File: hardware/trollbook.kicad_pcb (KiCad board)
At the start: 2 copper layers, 100 x 100 mm, 30 parts, among them U1 XC95288-208, U2 MC68030, U3 MC68882, U4 IDT71V416, U7 39F040, U8 MCP660

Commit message: dram
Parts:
- removed DB9FC: VAL**, DB9FC
- removed R10, R11, R12, R13, R14, R15, R16, R4, R5, R6, R7, R8, R9: R, SM0805
- added J2: VGAF, SUPER_CAP, F.Cu at (45.4, 237.8)
- added RP5: 10k, RPACK8_SMD, F.Cu at (73.5, 261.2)
- added RP6: 10k, RPACK8_SMD, F.Cu at (62.0, 246.7)
- added RP7: 10k, RPACK8_SMD, F.Cu at (72.6, 214.3)
- added RP8: 10k, RPACK8_SMD, F.Cu at (26.8, 232.6)
- added U10: 74LS574, SO20L, F.Cu at (80.4, 183.8)
- added U11: 74LS574, SO20L, B.Cu at (109.7, 169.3)
- added U12: HY57V561620, TSOP54, F.Cu at (178.1, 198.0)
- added U13: HY57V561620, TSOP54, F.Cu at (178.2, 182.5)
- added U6: 74LS574, SO20L, F.Cu at (98.1, 151.1)
- added U9: 74LS574, SO20L, B.Cu at (103.8, 195.5)
- R1, R2, R3: value R -> 10k
- RP1, RP2, RP3, RP4: value R_PACK4 -> 20k
- moved R19 153.4 mm to (16.1, 220.4)
- moved R17 153.4 mm to (41.3, 216.8)
- moved R18 153.4 mm to (34.4, 217.5)
- moved R2 153.4 mm to (16.0, 224.9)
- moved R3 153.4 mm to (27.5, 218.4)
- moved U8 153.4 mm to (37.1, 224.8)
- moved R1 153.4 mm to (16.3, 222.6)
- moved RP2 142.8 mm to (61.8, 252.3)
- moved RP4 140.0 mm to (61.0, 237.5)
- moved RP1 130.5 mm to (73.5, 264.8)
- moved RP3 126.7 mm to (72.5, 218.2)
- moved U4 1.95 mm to (106.9, 181.9)
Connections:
- R1 pad 1: N-0000013 -> N-00000162
- R1 pad 2: N-0000035 -> GND
- R2 pad 1: N-0000035 -> N-00000161
- R2 pad 2: N-0000090 -> GND
- R3 pad 1: N-0000090 -> N-00000160
- R3 pad 2: N-0000039 -> GND
- RP1 pad 1: (no net) -> N-000001
- RP1 pad 2: (no net) -> N-00000168
- RP1 pad 3: (no net) -> N-000005
- RP1 pad 4: (no net) -> N-00000167
- RP1 pad 5: N-0000039 -> /VGAB1
- RP1 pad 6: N-0000090 -> /VGAB2
- RP1 pad 7: N-0000035 -> /VGAB3
- RP1 pad 8: N-0000013 -> /VGAB4
- RP2 pad 1: (no net) -> N-00000166
- RP2 pad 2: (no net) -> N-000004
- RP2 pad 3: (no net) -> N-00000165
- RP2 pad 4: (no net) -> N-00000164
- RP2 pad 5: N-0000018 -> /VGAG3
- RP2 pad 6: N-000007 (its old number) -> /VGAG4
- RP2 pad 7: N-0000016 -> /VGAG5
- RP2 pad 8: N-0000017 -> /VGAB0
- RP3 pad 1: (no net) -> N-000002
- RP3 pad 2: (no net) -> N-00000163
- RP3 pad 3: (no net) -> N-00000159
- RP3 pad 4: (no net) -> N-000009
- RP3 pad 5: N-0000015 -> /VGAR4
- RP3 pad 6: N-0000010 (its old number) -> /VGAG0
- RP3 pad 7: N-000009 -> /VGAG1
- RP3 pad 8: N-000008 (its old number) -> /VGAG2
- RP4 pad 1: (no net) -> N-00000158
- RP4 pad 2: (no net) -> N-00000157
- RP4 pad 3: (no net) -> N-000003
- RP4 pad 4: (no net) -> N-00000169
- RP4 pad 5: N-0000012 (its old number) -> /VGAR0
- RP4 pad 6: N-0000091 -> /VGAR1
- RP4 pad 7: N-0000092 -> /VGAR2
- RP4 pad 8: N-0000011 (its old number) -> /VGAR3
- U1 pad 100: (no net) -> /FC1
- U1 pad 101: (no net) -> /FC2
- U1 pad 128: (no net) -> /DSACK0
- U1 pad 131: (no net) -> /DSACK1
- U1 pad 138: (no net) -> /CBACK
- U1 pad 139: (no net) -> /CBREQ
- U1 pad 140: (no net) -> /AS
- U1 pad 142: (no net) -> /DS
- U1 pad 164: (no net) -> /RW
- U1 pad 165: (no net) -> /SIZ1
- U1 pad 166: (no net) -> /SIZ0
- U1 pad 167: (no net) -> /DBEN
- U1 pad 99: (no net) -> /FC0
- U2 pad 10: (no net) -> /FC1
- U2 pad 117: (no net) -> /RW
- U2 pad 119: (no net) -> /SIZ1
- U2 pad 12: (no net) -> /FC0
- U2 pad 120: (no net) -> /SIZ0
- U2 pad 121: (no net) -> /DBEN
- U2 pad 124: (no net) -> /DS
- U2 pad 125: (no net) -> /AS
- U2 pad 126: (no net) -> /CBREQ
- U2 pad 127: (no net) -> /CBACK
- U2 pad 129: (no net) -> +5V
- U2 pad 132: (no net) -> /DSACK1
- U2 pad 17: (no net) -> +5V
- U2 pad 3: (no net) -> /DSACK0
- U2 pad 9: (no net) -> /FC2
- U3 pad 18: (no net) -> +5V
- U3 pad 20: (no net) -> /DS
- U3 pad 21: (no net) -> /AS
- U3 pad 26: /A0 -> +5V
- U3 pad 28: (no net) -> /RW
- U3 pad 31: (no net) -> /DSACK1
- U3 pad 32: (no net) -> /DSACK0
- U7 pad 31: (no net) -> /RW
- U8 pad 10: N-0000016 -> N-000004
- U8 pad 12: N-0000015 -> N-000009
- U8 pad 5: N-0000013 -> N-000001
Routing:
- net /RAMA11: track 0.00 -> 15.8 mm
- net /RAMA7: track 0.00 -> 15.8 mm
- net /RAMA2: track 0.00 -> 15.8 mm
- net /RAMD12: track 0.00 -> 15.8 mm
- net /RAMD11: track 0.00 -> 15.8 mm
- net /RAMB0: track 0.00 -> 15.8 mm
- net /RAMWE: track 0.00 -> 15.8 mm
- net /RAMLDQM: track 0.00 -> 15.8 mm
- net /RAMUDQM: track 0.00 -> 15.8 mm
- net /RAMD6: track 0.00 -> 15.8 mm
- net /RAMCKE: track 0.00 -> 15.8 mm
- net /RAMA12: track 0.00 -> 15.8 mm
- net /RAMD3: track 0.00 -> 15.8 mm
- net /RAMA8: track 0.00 -> 15.8 mm
- net /RAMD2: track 0.00 -> 15.8 mm
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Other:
- net class ninja added: clearance 0.1524, trace_width 0.1524, via_dia 0.7, via_drill 0.3
- rule trace_min: 0.2032 -> 0.1524

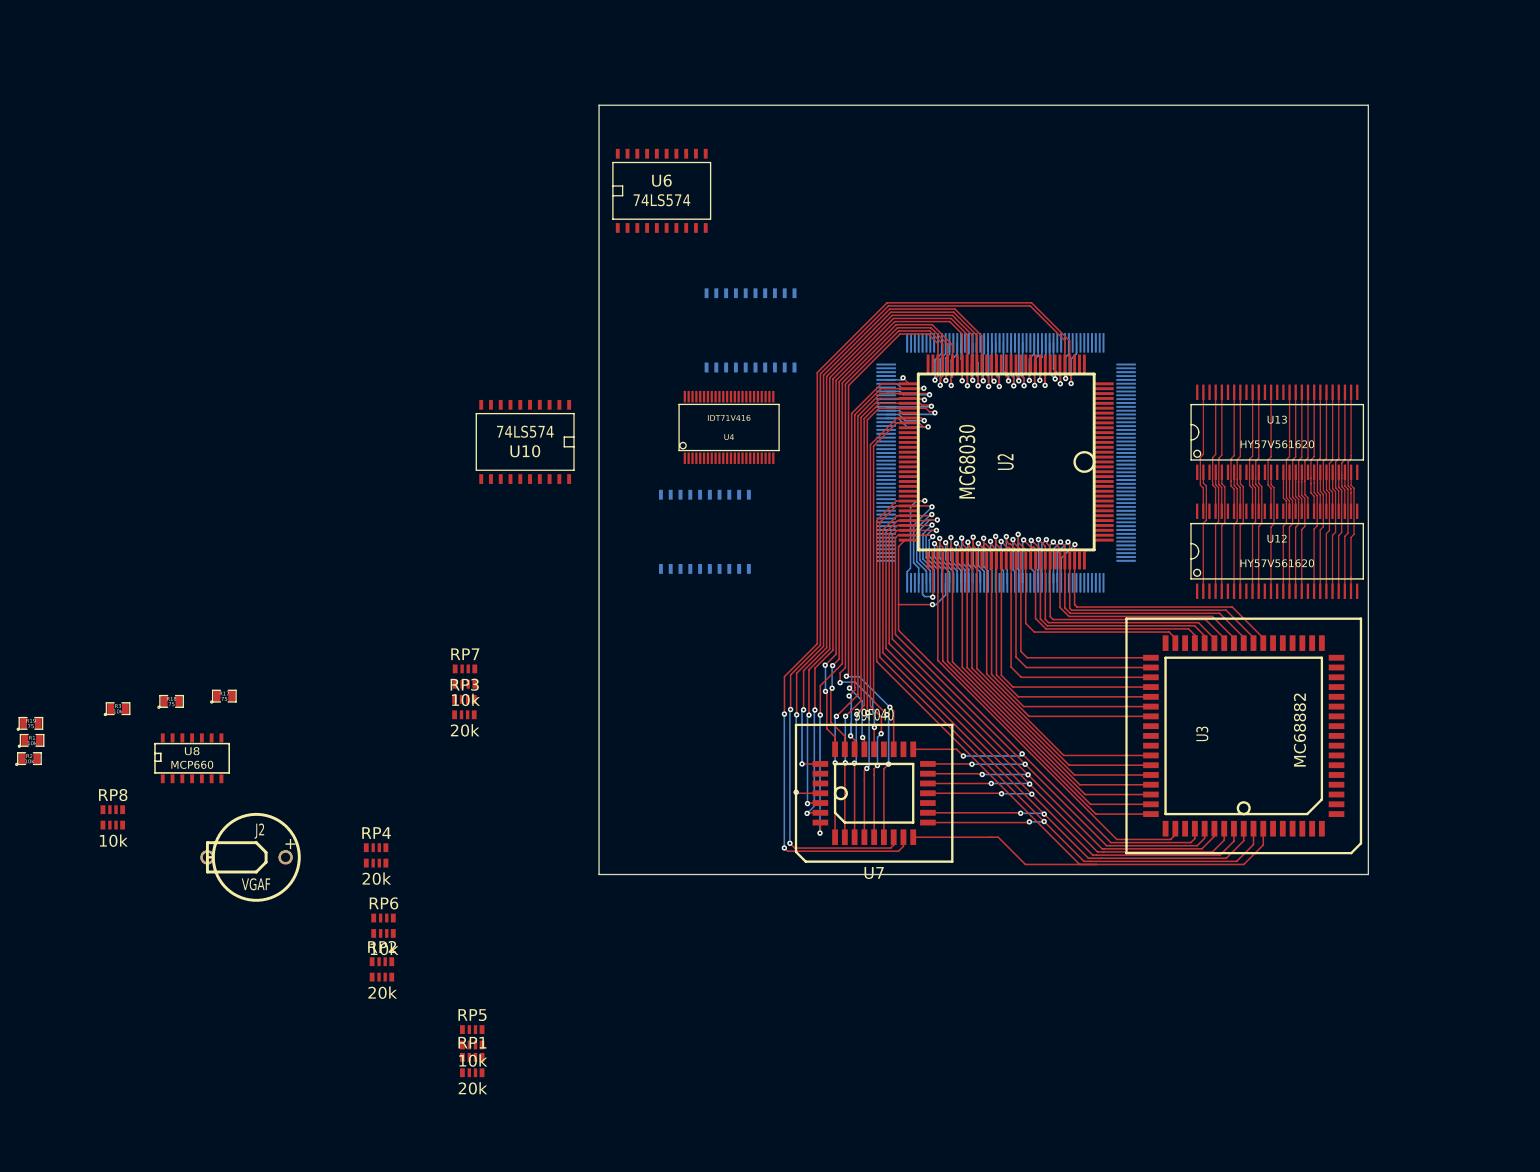
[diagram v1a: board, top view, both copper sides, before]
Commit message: routed sram, dram
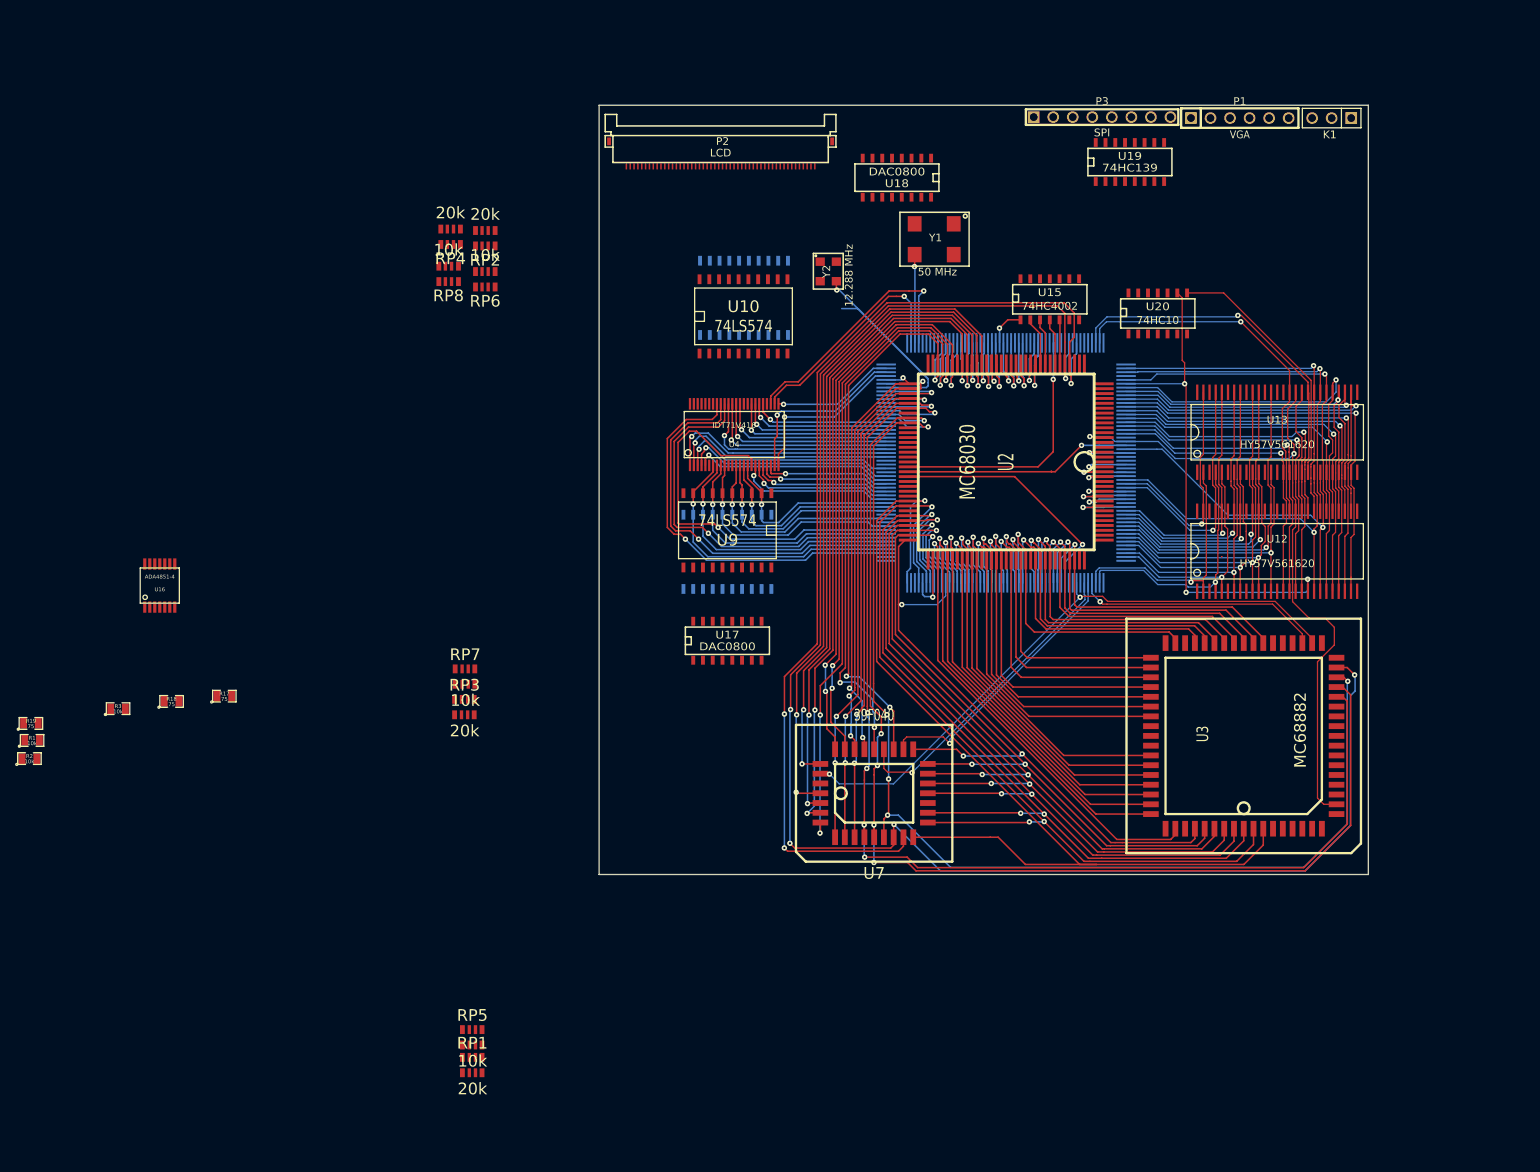
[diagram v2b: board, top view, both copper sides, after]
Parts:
- removed J2: VGAF, SUPER_CAP
- removed U8: MCP660, SO14E
- added K1: CONN_3, PIN_ARRAY_3X1, F.Cu at (185.2, 141.7)
- added P1: VGA, PIN_ARRAY-6X1, F.Cu at (173.3, 141.7)
- added P2: LCD, FH12-50S-0.5SH, F.Cu at (118.0, 147.4)
- added P3: SPI, pin_array_8x1, F.Cu at (155.4, 140.3)
- added U15: 74HC4002, SO14E, F.Cu at (148.6, 165.1)
- added U16: ADA4851-4, tssop-14, F.Cu at (32.9, 202.4)
- added U17: DAC0800, SO16E, F.Cu at (106.7, 209.6)
- added U18: DAC0800, SO16E, F.Cu at (128.7, 149.4)
- added U19: 74HC139, SO16E, F.Cu at (159.0, 147.4)
- added U20: 74HC10, SO14E, F.Cu at (162.6, 166.9)
- added Y1: 50 MHz, OSC-VCC1-B3B, F.Cu at (133.6, 157.4)
- added Y2: 12.288 MHz, OSC-ASFLMB, F.Cu at (119.8, 161.6)
- U6: moved to B.Cu
- U9: moved to F.Cu
- moved RP2 96.0 mm to (75.2, 157.3), turned to 180 degrees
- moved RP6 85.1 mm to (75.2, 162.6), turned to 180 degrees
- moved RP8 83.0 mm to (70.4, 161.9), turned to 180 degrees
- moved RP4 81.0 mm to (70.7, 157.1), turned to 180 degrees
- moved U6 47.7 mm to (106.7, 198.1)
- moved U10 32.7 mm to (108.8, 167.4), turned to 0 degrees
- moved U11 4.31 mm to (108.8, 165.0)
- moved U9 2.93 mm to (106.7, 195.3), turned to 180 degrees
- moved U4 1.15 mm to (107.6, 182.8)
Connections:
- U1 pad 100: /FC1 -> /SSBIN1
- U1 pad 101: /FC2 -> /CPUMODE
- U1 pad 102: (no net) -> /RAMA12
- U1 pad 103: (no net) -> /RAMUDQM
- U1 pad 106: (no net) -> /RAMA11
- U1 pad 107: (no net) -> /RAMA9
- U1 pad 109: (no net) -> /RAMA8
- U1 pad 110: (no net) -> /RAMCS0
- U1 pad 111: (no net) -> /RAMA7
- U1 pad 112: (no net) -> /RAMA6
- U1 pad 113: (no net) -> /RAMA5
- U1 pad 114: (no net) -> /RAMA4
- U1 pad 115: (no net) -> /RAMA3
- U1 pad 116: (no net) -> /RAMA2
- U1 pad 117: (no net) -> /RAMA1
- U1 pad 118: (no net) -> /RAMA0
- U1 pad 119: (no net) -> /RAMA10
- U1 pad 120: (no net) -> /RAMRAS
- U1 pad 121: (no net) -> /RAMCAS
- U1 pad 122: (no net) -> /RAMWE
- U1 pad 123: (no net) -> /RAMLDQM
- U1 pad 125: (no net) -> /CPUCLK
- U1 pad 126: (no net) -> /IPL1
- U1 pad 127: (no net) -> /RAMB1
- U1 pad 133: (no net) -> /STERM
- U1 pad 134: (no net) -> /BERR
- U1 pad 135: (no net) -> /RAMB0
- U1 pad 136: (no net) -> /RAMD15
- U1 pad 137: (no net) -> /RAMD14
- U1 pad 143: (no net) -> /RAMD13
- U1 pad 144: (no net) -> /RAMD12
- U1 pad 145: (no net) -> /RAMD11
- U1 pad 146: (no net) -> /RAMD10
- U1 pad 147: (no net) -> /RAMD9
- U1 pad 148: (no net) -> /RAMD8
- U1 pad 149: (no net) -> /RAMD7
- U1 pad 150: (no net) -> /RAMD6
- U1 pad 151: (no net) -> /RAMD5
- U1 pad 152: (no net) -> /RAMD4
- U1 pad 154: (no net) -> /RAMD3
- U1 pad 155: (no net) -> /RAMD2
- U1 pad 158: (no net) -> /RAMD1
- U1 pad 159: (no net) -> /RAMD0
- U1 pad 160: (no net) -> /FPUCS
- U1 pad 161: (no net) -> /ROMCE
- U1 pad 162: (no net) -> /ROMOE
- U1 pad 167: /DBEN -> /IPL0
- U1 pad 17: /LLA10 -> /LLA6
- U1 pad 18: /LLA9 -> /LLA7
- U1 pad 20: /LLA7 -> /LLA9
- U1 pad 206: (no net) -> /RESET
- U1 pad 21: /LLA6 -> /LLA10
- U1 pad 3: (no net) -> /LLOE
- U1 pad 46: (no net) -> /CLK12
- U1 pad 49: /LLA11 -> /LLA12
- U1 pad 5: (no net) -> /LLBHE
- U1 pad 50: /LLA12 -> /LLA11
- U1 pad 55: (no net) -> /CLK50
- U1 pad 61: (no net) -> /VGALATCH
- U1 pad 7: (no net) -> /LLBLE
- U1 pad 72: (no net) -> /SNDLATCH
- U1 pad 77: (no net) -> /ATOOHIGH
- U1 pad 84: (no net) -> /VGAVSYNC
- U1 pad 85: (no net) -> /VGAHSYNC
- U1 pad 88: /A28 -> /SPICLK
- U1 pad 89: /A29 -> /SPIMISO
- U1 pad 9: (no net) -> /LLWEN
- U1 pad 90: /A30 -> /SPIMOSI
- U1 pad 91: /A31 -> /IPL2
- U1 pad 99: /FC0 -> /SSBIN0
- U10 pad 1: (no net) -> /VGAOE
- U10 pad 11: (no net) -> /VGALATCH
- U10 pad 12: /VGAR4 -> /VGAG3
- U10 pad 13: /VGAR3 -> /VGAG4
- U10 pad 14: /VGAR2 -> /VGAG5
- U10 pad 15: /VGAR1 -> /VGAR0
- U10 pad 16: /VGAR0 -> /VGAR1
- U10 pad 17: /VGAG5 -> /VGAR2
- U10 pad 18: /VGAG4 -> /VGAR3
- U10 pad 19: /VGAG3 -> /VGAR4
- U10 pad 2: /LLD8 -> /LLD15
- U10 pad 20: GND -> VCC
- U10 pad 3: /LLD9 -> /LLD14
- U10 pad 4: /LLD10 -> /LLD13
- U10 pad 5: /LLD11 -> /LLD12
- U10 pad 6: /LLD12 -> /LLD11
- U10 pad 7: /LLD13 -> /LLD10
- U10 pad 8: /LLD14 -> /LLD9
- U10 pad 9: /LLD15 -> /LLD8
- U11 pad 1: (no net) -> GND
- U11 pad 11: (no net) -> /SNDLATCH
- U11 pad 12: (no net) -> N-00000138
- U11 pad 13: (no net) -> N-00000134
- U11 pad 14: (no net) -> N-00000135
- U11 pad 15: (no net) -> N-00000136
- U11 pad 16: (no net) -> N-00000137
- U11 pad 17: (no net) -> N-00000133
- U11 pad 18: (no net) -> N-00000139
- U11 pad 19: (no net) -> N-00000140
- U11 pad 20: GND -> VCC
- U12 pad 19: (no net) -> /RAMCS0
- U12 pad 37: /RAMCKE -> 3V3
- U12 pad 38: /RAMCLK -> /CPUCLK
- U13 pad 19: (no net) -> /RAMCS1
- U13 pad 37: /RAMCKE -> 3V3
- U13 pad 38: /RAMCLK -> /CPUCLK
- U2 pad 121: /DBEN -> (no net)
- U2 pad 130: (no net) -> /BERR
- U2 pad 131: (no net) -> /STERM
- U2 pad 6: (no net) -> /CPUCLK
- U2 pad 64: (no net) -> /RESET
- U2 pad 68: (no net) -> /IPL2
- U2 pad 69: (no net) -> /IPL1
- U2 pad 7: (no net) -> GND
- U2 pad 70: (no net) -> /IPL0
- U3 pad 11: (no net) -> /CPUCLK
- U3 pad 14: GND -> /RESET
- U3 pad 29: (no net) -> /FPUCS
- U4 pad 17: (no net) -> /LLWEN
- U4 pad 39: (no net) -> /LLBLE
- U4 pad 40: (no net) -> /LLBHE
- U4 pad 41: (no net) -> /LLOE
- U4 pad 6: (no net) -> GND
- U6 pad 1: (no net) -> GND
- U6 pad 11: (no net) -> /SNDLATCH
- U6 pad 12: (no net) -> N-00000142
- U6 pad 13: (no net) -> N-00000143
- U6 pad 14: (no net) -> N-00000144
- U6 pad 15: (no net) -> N-00000145
- U6 pad 16: (no net) -> N-00000141
- U6 pad 17: (no net) -> N-00000146
- U6 pad 18: (no net) -> N-00000147
- U6 pad 19: (no net) -> N-00000148
- U6 pad 20: GND -> VCC
- U7 pad 22: (no net) -> /ROMCE
- U7 pad 24: (no net) -> /ROMOE
- U9 pad 1: (no net) -> /VGAOE
- U9 pad 11: (no net) -> /VGALATCH
- U9 pad 12: /VGAG2 -> /VGAB0
- U9 pad 13: /VGAG1 -> /VGAB1
- U9 pad 14: /VGAG0 -> /VGAB2
- U9 pad 15: /VGAB4 -> /VGAB3
- U9 pad 16: /VGAB3 -> /VGAB4
- U9 pad 17: /VGAB2 -> /VGAG0
- U9 pad 18: /VGAB1 -> /VGAG1
- U9 pad 19: /VGAB0 -> /VGAG2
- U9 pad 2: /LLD0 -> /LLD7
- U9 pad 20: GND -> VCC
- U9 pad 3: /LLD1 -> /LLD6
- U9 pad 4: /LLD2 -> /LLD5
- U9 pad 5: /LLD3 -> /LLD4
- U9 pad 6: /LLD4 -> /LLD3
- U9 pad 7: /LLD5 -> /LLD2
- U9 pad 8: /LLD6 -> /LLD1
- U9 pad 9: /LLD7 -> /LLD0
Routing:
- net /CPUCLK: track 0.00 -> 91.0 mm, vias 0 -> 2
- net /A1: track 124.7 -> 215.3 mm, vias 3 -> 5
- net /A3: track 65.9 -> 156.5 mm, vias 3 -> 5
- net /A4: track 70.9 -> 158.6 mm, vias 3 -> 5
- net /A2: track 66.4 -> 151.5 mm, vias 3 -> 5
- net /RW: track 0.00 -> 79.5 mm, vias 0 -> 2
- net /RAMCS0: track 0.00 -> 66.0 mm, vias 0 -> 3
- net /LLWEN: track 0.00 -> 51.4 mm, vias 0 -> 1
- net /LLOE: track 0.00 -> 51.3 mm, vias 0 -> 1
- net /LLBHE: track 0.00 -> 50.7 mm, vias 0 -> 1
- net /LLBLE: track 0.00 -> 49.9 mm, vias 0 -> 1
- net /ROMOE: track 0.00 -> 40.4 mm, vias 0 -> 1
- net /CLK12: track 0.00 -> 39.3 mm, vias 0 -> 1
- net /RAMA3: track 15.8 -> 54.2 mm, vias 0 -> 1
- net /LLD0: track 0.00 -> 37.3 mm, vias 0 -> 1
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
